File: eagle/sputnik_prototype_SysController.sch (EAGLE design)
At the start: 62 parts, among them U1 MEGA128-M, Y2 8MHZ

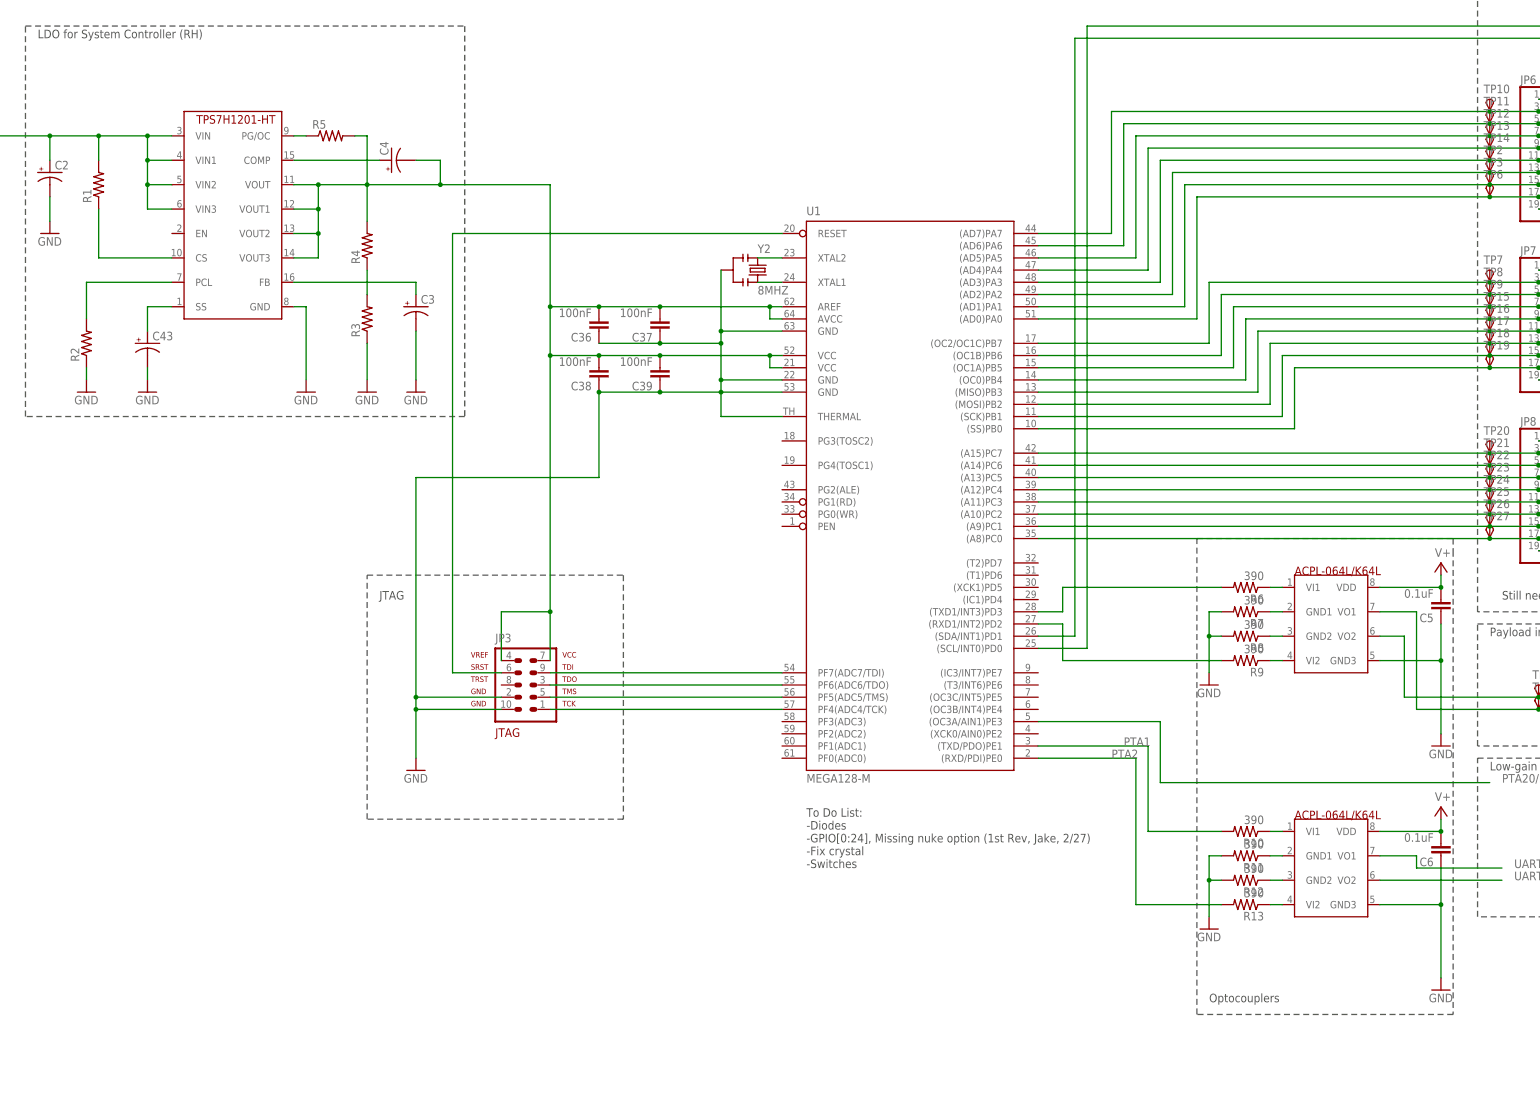
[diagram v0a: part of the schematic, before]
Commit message: added attributes, replaced atmega footprint with correct version, replaced resonator with xtal
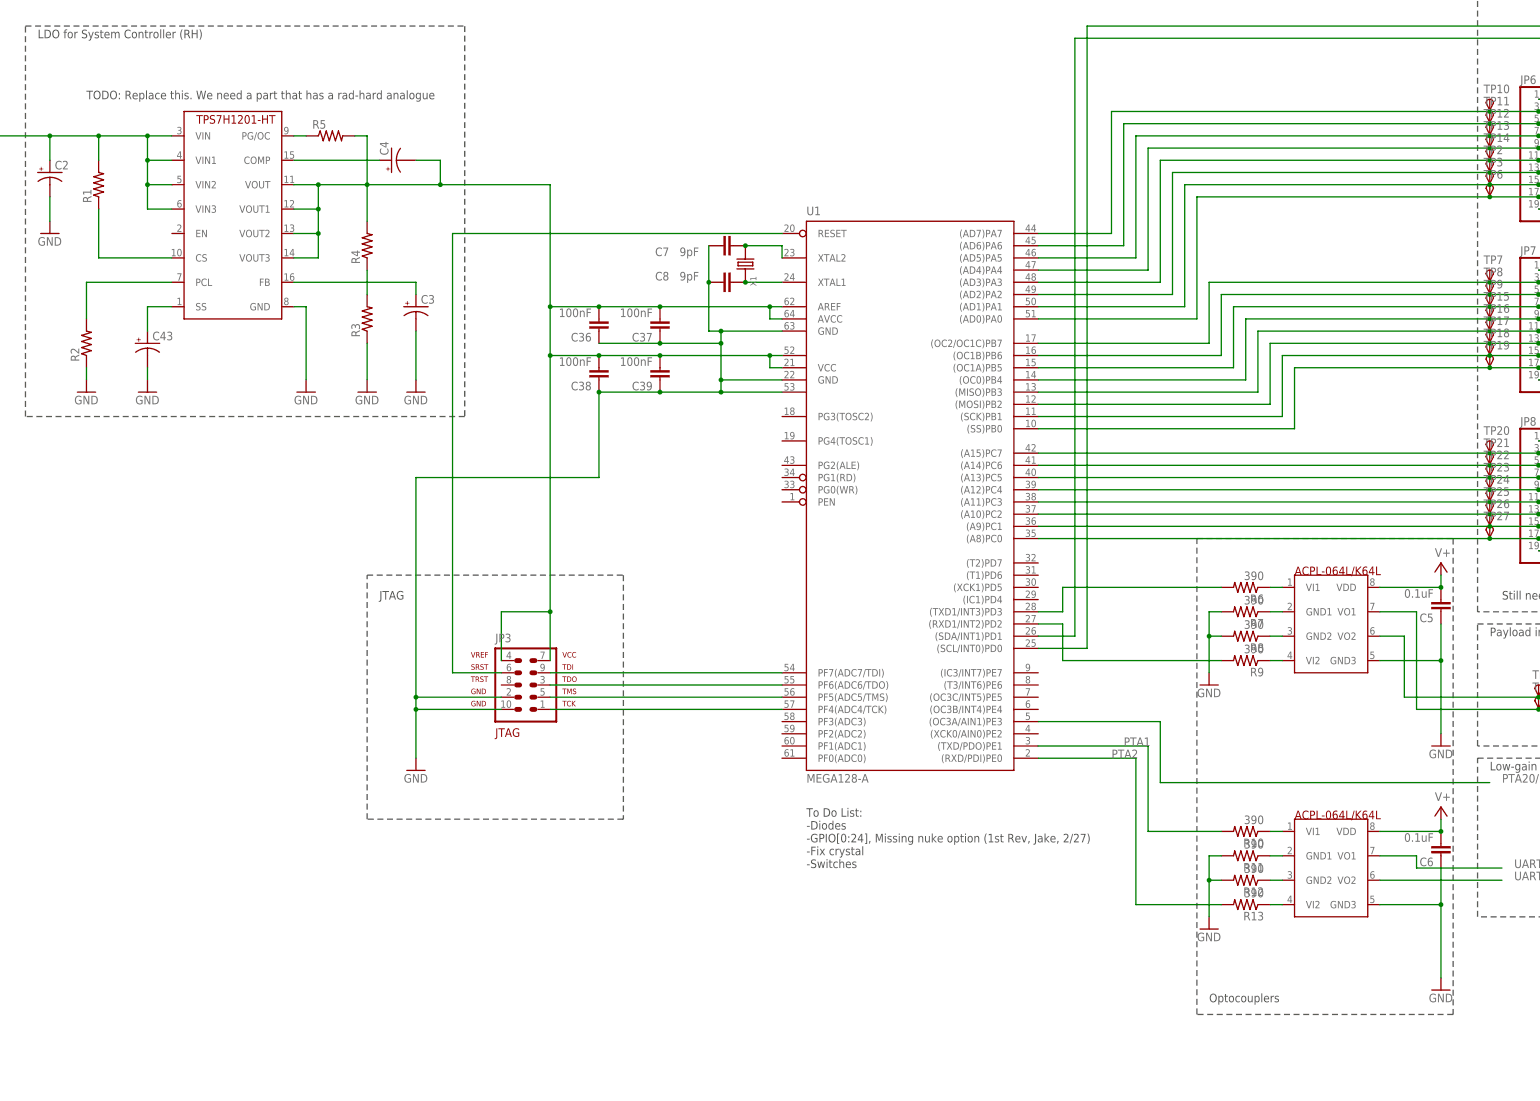
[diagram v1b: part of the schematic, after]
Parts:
- removed Y2: 8MHZ, Lilypad_Arduino_USB_v12:SPARKFUN-FREQCTRL_RESONATOR8MHZ
- added C7, C8: 9pF, rcl_custom:C-EU0603-B-NOSILK
- added X1: (no value), monitor-v2:CRYSTAL-3.2X1.5-A
- U1: value MEGA128-M -> MEGA128-A; device atmel:MEGA128-M -> atmel:MEGA128-A; MFN (none) -> Atmel; MPN (none) -> atmega128
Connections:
- removed net N$23: U1.XTAL2, Y2.1
- removed net N$36: U1.XTAL1, Y2.3
- new net N$17: C7.2, U1.XTAL2, X1.1
- new net N$22: C8.2, U1.XTAL1, X1.2
- net GND: now also C7.1, C8.1, U1.GND1; no longer U1.GND@2, U1.THERMAL, Y2.2
- net N$1: now also U1.VCC1; no longer U1.VCC@1
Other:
- note added: "TODO: Replace this. We need a part that has a rad-hard analogue"
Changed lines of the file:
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@@
 <?xml version="1.0" encoding="utf-8"?>
 <!DOCTYPE eagle SYSTEM "eagle.dtd">
-<eagle version="7.4.0">
+<eagle version="7.3.0">
 <drawing>
 <settings>
@@
 <parts>
 <part name="FRAME1" library="frames" deviceset="FRAME_C_L" device=""/>
-<part name="U1" library="atmel" deviceset="MEGA128-M" device=""/>
+<part name="U1" library="atmel" deviceset="MEGA128" device="-A">
+<attribute name="MFN" value="Atmel"/>
+<attribute name="MPN" value="atmega128"/>
+</part>
 <part name="JP1" library="psas_c3_team05" deviceset="PINHD-1X2" device=""/>
 <part name="JP2" library="psas_c3_team05" deviceset="PINHD-1X2" device=""/>
@@
 <part name="C38" library="rcl_custom" deviceset="C-EU" device="0603-B-NOSILK" value="100nF"/>
 <part name="C39" library="rcl_custom" deviceset="C-EU" device="0603-B-NOSILK" value="100nF"/>
-<part name="Y2" library="Lilypad_Arduino_USB_v12" deviceset="SPARKFUN-FREQCTRL_RESONATOR" device="8MHZ" value="8MHZ"/>
 <part name="JP5" library="psas_c3_team05" deviceset="PINHD-1X2" device=""/>
 <part name="SUPPLY12" library="psas_c3_team05" deviceset="V+" device=""/>
@@
 <part name="GND16" library="psas_c3_team05" deviceset="GND" device=""/>
 <part name="C6" library="rcl_custom" deviceset="C-EU" device="0603-B-NOSILK" value="0.1uF"/>
+<part name="X1" library="monitor-v2" deviceset="CRYSTAL" device="-3.2X1.5-A">
+<attribute name="DIST" value="Digi-Key"/>
+<attribute name="DPN" value="535-10630-1-ND"/>
+<attribute name="MFN" value="Abracon LLC"/>
+<attribute name="MPN" value="ABM3-8.00MHZ-D2Y-T"/>
+</part>
+<part name="C7" library="rcl_custom" deviceset="C-EU" device="0603-B-NOSILK" value="9pF"/>
+<part name="C8" library="rcl_custom" deviceset="C-EU" device="0603-B-NOSILK" value="9pF"/>
 </parts>
 <sheets>
@@
 <wire x1="195.58" y1="147.32" x2="195.58" y2="198.12" width="0.1524" layer="97" style="longdash"/>
 <text x="198.12" y="193.04" size="1.778" layer="97">JTAG</text>
-<wire x1="421.64" y1="203.2" x2="421.64" y2="106.68" width="0.1524" layer="97" style="longdash"/>
+<wire x1="421.64" y1="205.74" x2="421.64" y2="106.68" width="0.1524" layer="97" style="longdash"/>
 <wire x1="421.64" y1="106.68" x2="368.3" y2="106.68" width="0.1524" layer="97" style="longdash"/>
 <wire x1="368.3" y1="106.68" x2="368.3" y2="205.74" width="0.1524" layer="97" style="longdash"/>
 <wire x1="368.3" y1="205.74" x2="421.64" y2="205.74" width="0.1524" layer="97" style="longdash"/>
-<wire x1="421.64" y1="205.74" x2="421.64" y2="203.2" width="0.1524" layer="97" style="longdash"/>
 <text x="370.84" y="109.22" size="1.778" layer="97">Optocouplers</text>
+<text x="137.16" y="297.18" size="1.778" layer="97">TODO: Replace this. We need a part that has a rad-hard analogue</text>
 </plain>
 <instances>
 <instance part="FRAME1" gate="G$1" x="0" y="0"/>
 <instance part="FRAME1" gate="G$2" x="325.12" y="0"/>
-<instance part="U1" gate="G$1" x="309.88" y="215.9"/>
+<instance part="U1" gate="G$1" x="309.88" y="215.9">
+<attribute name="MFN" x="309.88" y="215.9" size="1.778" layer="96" display="off"/>
+<attribute name="MPN" x="309.88" y="215.9" size="1.778" layer="96" display="off"/>
+</instance>
 <instance part="JP1" gate="G$1" x="444.5" y="325.12" rot="MR0"/>
 <instance part="JP2" gate="G$1" x="444.5" y="309.88" rot="MR0"/>
@@
 <instance part="C38" gate="CE" x="243.84" y="238.76" rot="R180"/>
 <instance part="C39" gate="CE" x="256.54" y="238.76" rot="R180"/>
-<instance part="Y2" gate="G$1" x="276.86" y="261.62" smashed="yes" rot="R270">
-<attribute name="NAME" x="276.86" y="265.176" size="1.778" layer="95"/>
-<attribute name="VALUE" x="276.86" y="256.54" size="1.778" layer="96"/>
-</instance>
 <instance part="JP5" gate="G$1" x="459.74" y="170.18"/>
 <instance part="SUPPLY12" gate="1" x="73.66" y="299.72"/>
@@
 <instance part="GND16" gate="1" x="419.1" y="111.76"/>
 <instance part="C6" gate="CE" x="419.1" y="139.7" rot="R180"/>
+<instance part="X1" gate="X" x="274.32" y="261.62" rot="R270">
+<attribute name="MFN" x="274.32" y="261.62" size="1.778" layer="96" rot="R270" display="off"/>
+<attribute name="MPN" x="274.32" y="261.62" size="1.778" layer="96" rot="R270" display="off"/>
+<attribute name="DIST" x="274.32" y="261.62" size="1.778" layer="96" rot="R270" display="off"/>
+<attribute name="DPN" x="274.32" y="261.62" size="1.778" layer="96" rot="R270" display="off"/>
+</instance>
+<instance part="C7" gate="CE" x="269.24" y="266.7" smashed="yes" rot="R90">
+<attribute name="NAME" x="255.524" y="264.541" size="1.778" layer="95"/>
+<attribute name="VALUE" x="260.604" y="264.541" size="1.778" layer="96"/>
+</instance>
+<instance part="C8" gate="CE" x="269.24" y="259.08" smashed="yes" rot="R90">
+<attribute name="NAME" x="255.524" y="259.461" size="1.778" layer="95"/>
+<attribute name="VALUE" x="260.604" y="259.461" size="1.778" layer="96"/>
+</instance>
 </instances>
 <busses>
@@
 <wire x1="281.94" y1="238.76" x2="269.24" y2="238.76" width="0.1524" layer="91"/>
 <junction x="269.24" y="238.76"/>
-<pinref part="U1" gate="G$1" pin="GND@2"/>
+<pinref part="U1" gate="G$1" pin="GND1"/>
 <wire x1="281.94" y1="236.22" x2="269.24" y2="236.22" width="0.1524" layer="91"/>
 <wire x1="269.24" y1="236.22" x2="256.54" y2="236.22" width="0.1524" layer="91"/>
@@
 <pinref part="C39" gate="CE" pin="1"/>
 <junction x="256.54" y="236.22"/>
-<pinref part="Y2" gate="G$1" pin="2"/>
-<wire x1="269.24" y1="261.62" x2="269.24" y2="248.92" width="0.1524" layer="91"/>
-<junction x="269.24" y="248.92"/>
-<pinref part="U1" gate="G$1" pin="THERMAL"/>
-<wire x1="281.94" y1="231.14" x2="269.24" y2="231.14" width="0.1524" layer="91"/>
-<wire x1="269.24" y1="231.14" x2="269.24" y2="236.22" width="0.1524" layer="91"/>
 <wire x1="205.74" y1="218.44" x2="243.84" y2="218.44" width="0.1524" layer="91"/>
 <wire x1="243.84" y1="218.44" x2="243.84" y2="236.22" width="0.1524" layer="91"/>
 <junction x="243.84" y="236.22"/>
+<pinref part="C7" gate="CE" pin="1"/>
+<pinref part="C8" gate="CE" pin="1"/>
+<wire x1="266.7" y1="259.08" x2="266.7" y2="266.7" width="0.1524" layer="91"/>
+<wire x1="266.7" y1="259.08" x2="266.7" y2="248.92" width="0.1524" layer="91"/>
+<junction x="266.7" y="259.08"/>
+<wire x1="266.7" y1="248.92" x2="269.24" y2="248.92" width="0.1524" layer="91"/>
+<junction x="269.24" y="248.92"/>
 </segment>
 <segment>
@@
 <pinref part="JP3" gate="G$1" pin="6"/>
 <wire x1="213.36" y1="177.8" x2="223.52" y2="177.8" width="0.1524" layer="91"/>
-</segment>
-</net>
-<net name="N$23" class="0">
-<segment>
-<pinref part="U1" gate="G$1" pin="XTAL2"/>
-<pinref part="Y2" gate="G$1" pin="1"/>
-<wire x1="276.86" y1="264.16" x2="281.94" y2="264.16" width="0.1524" layer="91"/>
-</segment>
-</net>
-<net name="N$36" class="0">
-<segment>
-<pinref part="U1" gate="G$1" pin="XTAL1"/>
-<pinref part="Y2" gate="G$1" pin="3"/>
-<wire x1="276.86" y1="259.08" x2="281.94" y2="259.08" width="0.1524" layer="91"/>
 </segment>
 </net>
@@
 <wire x1="243.84" y1="243.84" x2="256.54" y2="243.84" width="0.1524" layer="91"/>
 <junction x="243.84" y="243.84"/>
-<pinref part="U1" gate="G$1" pin="VCC@1"/>
+<pinref part="U1" gate="G$1" pin="VCC1"/>
 <wire x1="256.54" y1="243.84" x2="279.4" y2="243.84" width="0.1524" layer="91"/>
 <junction x="256.54" y="243.84"/>
@@
 </segment>
 </net>
+<net name="N$17" class="0">
+<segment>
+<pinref part="X1" gate="X" pin="1"/>
+<pinref part="C7" gate="CE" pin="2"/>
+<pinref part="U1" gate="G$1" pin="XTAL2"/>
+<wire x1="274.32" y1="266.7" x2="281.94" y2="266.7" width="0.1524" layer="91"/>
+<wire x1="281.94" y1="266.7" x2="281.94" y2="264.16" width="0.1524" layer="91"/>
+<junction x="274.32" y="266.7"/>
+</segment>
+</net>
+<net name="N$22" class="0">
+<segment>
+<pinref part="X1" gate="X" pin="2"/>
+<pinref part="C8" gate="CE" pin="2"/>
+<pinref part="U1" gate="G$1" pin="XTAL1"/>
+<wire x1="274.32" y1="259.08" x2="281.94" y2="259.08" width="0.1524" layer="91"/>
+<junction x="274.32" y="259.08"/>
+</segment>
+</net>

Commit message: Got rid of SysCon LDO, fixed Optoisolator symbol
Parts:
- removed C2, C3, C4, C43: (no value), rcl:CPOL-USCT6032
- removed R11, R7: 390, rcl_custom:R-US_0603-B-NOSILK
- removed R3, R4, R5: (no value), rcl_custom:R-US_0603-B-NOSILK
- removed U$3: ACPL-064L/K64L, psas_c3_team05:ACPL-064L/K64L
- R1, R2: value (none) -> 390
- U$1: value TPS7H1201-HT -> ACPL-064L/K64L; device psas_c3_team05:TPS7H1201-HT -> psas_c3_team05:ACPL-064L/K64L
- U1: MPN atmega128 -> (none)
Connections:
- removed net N$16: R9.2, U1.(RXD1/INT2)PD2
- removed net N$27: R11.1, U$3.GND1
- removed net N$5: C4.+, U$1.COMP
- removed net N$6: R3.2, R4.1
- removed net N$7: R5.1, U$1.PG/OC
- removed net N$8: R2.2, U$1.PCL
- removed net N$9: R1.1, U$1.CS
- removed net UART0_TX: U$3.VO2
- new net N$36: C1.+
- net GND: now also R13.2, R9.2, U$1.GND3, U1.GND@2; no longer C2.-, C3.-, C43.-, R11.2, R2.1, R3.1, R7.2, U$1.GND, U$3.GND3, U1.GND1
- net N$1: now also U1.VCC@1; no longer C4.-, R4.2, R5.2, U$1.VOUT, U$1.VOUT1, U$1.VOUT2, U$1.VOUT3, U1.VCC1
- net N$19: now also U$2.VO2, U1.(RXD1/INT2)PD2; no longer R7.1, U$2.GND1
- net N$2: now also R1.1; no longer C43.+, U$1.SS
- net N$20: now also U$2.GND1; no longer U$2.GND2
- net N$21: now also U$2.GND2; no longer U$2.VI2
- net N$26: now also U$1.VI1; no longer U$3.VI1
- net N$28: now also U$1.GND1; no longer U$3.GND2
- net N$29: now also U$1.GND2; no longer U$3.VI2
- net N$3: now also JP5.1, R2.1, TP4.PP; no longer C1.+, C2.+, R1.2, U$1.VIN, U$1.VIN1, U$1.VIN2, U$1.VIN3
- net N$4: now also U$1.VI2; no longer C3.+, U$1.FB
- net PTA2: now also U$1.VO2; no longer R13.2
- net UART0_RX: now also R1.2, U$1.VO1; no longer U$3.VO1
- net UART1_RX: now also R2.2, U$2.VO1; no longer JP5.1, TP4.PP, U$2.VO2
- net UART1_TX: now also U$2.VI2; no longer U$2.VO1
- net V+: now also U$1.VDD; no longer U$3.VDD
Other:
- moved on the sheet: JP5, R1, R2, TP4, TP5

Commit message: Fixed OIs, fixed SysCon LDO, replaced SPI cache
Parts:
- removed R12: 390, rcl_custom:R-US_0603-B-NOSILK
- added C2, C3: 0.1uF, rcl_custom:C-EU0603-B-NOSILK
- added C4: 2.2uF, rcl_custom:C-EU0402-B-NOSILK
- added C40: 10nF, rcl_custom:C-EU0402-B-NOSILK
- added C41: 1uF, rcl_custom:C-EU0402-B-NOSILK
- added R11, R3, R4, R5, R7: 390, rcl_custom:R-US_0603-B-NOSILK
- added U$3, U$4: ACPL-M61L, psas_c3_team05:ACPL-M61L
- added U$8: AAT3215, psas_c3_team05:AAT3215
- U$1, U$2: value ACPL-064L/K64L -> ACPL-M61L; device psas_c3_team05:ACPL-064L/K64L -> psas_c3_team05:ACPL-M61L
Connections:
- net N$2 renamed PTA1/UART0_RX
- removed net N$1: C36.2, C37.2, C38.2, C39.2, JP3.4, JP3.7, U1.AREF, U1.AVCC, U1.VCC, U1.VCC@1
- removed net N$26: R10.1, U$1.VI1
- removed net N$28: R12.1, U$1.GND1
- removed net N$29: R13.1, U$1.GND2
- removed net UART0_RX: R1.2, U$1.VO1
- new net N$16: R1.2, U$3.VOUT
- new net N$2: C36.2, C37.2, C38.2, C39.2, C4.1, JP3.4, JP3.7, U$8.VOUT, U1.AREF, U1.AVCC, U1.VCC, U1.VCC@1
- new net N$23: C40.1, U$8.BYP
- new net N$24: R11.1, U$2.VOUT
- new net N$5: R2.2, U$1.VOUT
- new net N$6: R3.1, U$1.VIN
- new net N$7: R4.1, U$1.GND1
- new net N$8: R5.2, U$2.VIN
- new net N$9: R6.1
- new net PTA2/UART1_TX: R10.1
- net GND: now also C2.1, C3.1, C4.2, C40.2, C41.2, R4.2, R6.2, U$1.GND2, U$2.GND2, U$3.GND2, U$4.GND2, U$8.GND; no longer R12.2, R8.2, U$1.GND3, U$2.GND3
- net N$10: now also R3.2; no longer R6.2
- net N$18: now also R8.1, U$4.VOUT; no longer R6.1, U$2.VI1
- net N$19: now also R11.2; no longer U$2.VO2
- net N$20: now also R10.2, U$4.VIN; no longer R8.1, U$2.GND1
- net N$21: now also U$4.GND1; no longer U$2.GND2
- net N$3: now also R13.1, U$3.GND1; no longer JP5.1, R2.1, TP4.PP
- net N$36: now also C41.1, U$8.VIN
- net N$4: now also R7.1, U$3.VIN; no longer U$1.VI2
- net PTA1: now also R7.2; no longer R10.2
- net PTA2: now also R8.2; no longer U$1.VO2
- net UART1_RX: now also JP5.1, R2.1, TP4.PP; no longer R2.2, U$2.VO1
- net UART1_TX: now also R5.1; no longer U$2.VI2
- net V+: now also C2.2, C3.2, U$3.VDD, U$4.VDD
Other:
- moved on the sheet: C1, C6, R1, R10, R13, R6, R8, R9

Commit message: Had to fix to do again because I'm a dumbass
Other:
- note added: "To Do List: -Diodes -GPIO[0:24], Missing nuke option (1st Rev, Jake, 2/27) -Fix crystal -Switches -Fix OI grounds"
- note removed: "To Do List: -Diodes -GPIO[0:24], Missing nuke option (1st Rev, Jake, 2/27) -Fix crystal -Switches"
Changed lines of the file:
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@@
 -GPIO[0:24], Missing nuke option (1st Rev, Jake, 2/27)
 -Fix crystal
--Switches</text>
+-Switches
+-Fix OI grounds</text>
 <text x="464.82" y="287.02" size="1.778" layer="97">GPIO</text>
 <text x="464.82" y="248.92" size="1.778" layer="97">GPIO</text>
